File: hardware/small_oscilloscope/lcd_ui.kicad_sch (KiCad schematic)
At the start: 9 parts, among them SW1 RotaryEncoder_Switch_MP, SW2 RotaryEncoder_Switch_MP, SW3 SW_MEC_5E, SW4 SW_MEC_5E, SW5 SW_MEC_5E

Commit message: 250627 circuit
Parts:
- added D4, D5, D6, D7: LED, LED_THT:LED_D3.0mm, symbol Device:LED
- added R29, R30, R31, R32: 1k, Resistor_SMD:R_0603_1608Metric_Pad0.98x0.95mm_HandSolder, symbol Device:R
- added R35, R36, R37, R40, R41, R42: 10k, Resistor_SMD:R_0402_1005Metric_Pad0.72x0.64mm_HandSolder, symbol Device:R
- added SW1: SW_MEC_5E, Button_Switch_SMD:SW_SPST_CK_KMS2xxGP, symbol Switch:SW_MEC_5E
- R33: renamed from R30; footprint (none) -> Resistor_SMD:R_0402_1005Metric_Pad0.72x0.64mm_HandSolder
- R34: renamed from R29; footprint (none) -> Resistor_SMD:R_0402_1005Metric_Pad0.72x0.64mm_HandSolder
- R38: renamed from R31; footprint (none) -> Resistor_SMD:R_0402_1005Metric_Pad0.72x0.64mm_HandSolder
- R39: renamed from R32; footprint (none) -> Resistor_SMD:R_0402_1005Metric_Pad0.72x0.64mm_HandSolder
- renumbered SW1 to SW2, SW5 to SW4, SW4 to SW5, SW2 to SW6
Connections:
- net +3.3V: now also R29.2, R30.2, R31.2, R32.2, R35.1, R36.1, R37.1, R40.1, R41.1, R42.1
- net GND: now also SW2.MP, SW2.S2, SW3.3 (K), SW3.4 (A), SW4.3 (K), SW4.4 (A), SW5.3 (K), SW5.4 (A), SW6.MP, SW6.S2, SW1.3 (K), SW1.4 (A)
- net RE1A: now reaches R39.2, SW6.A
- net RE0A: now reaches R34.2, SW2.A
- net RE0B: now reaches R33.2, SW2.B
- net RE0P: now reaches SW2.S1
- net RE0P: now also R36.2
- net RE1B: now reaches R38.2, SW6.B
- net SW2: now reaches SW4.1
- net SW2: now also SW4.2, R40.2
- net SW0: now reaches SW3.1
- net SW0: now also SW3.2, R37.2
- net RE1P: now reaches SW6.S1
- net RE1P: now also R42.2
- net SW1: now reaches SW5.1
- net SW1: now also SW5.2, R41.2
- new net: D5.1 (K), R30.1
- new net: D4.1 (K), R29.1
- new net: D6.1 (K), R31.1
- new net: D7.1 (K), R32.1
- new net LED0: D4.2 (A)
- new net LED1: D5.2 (A)
- new net LEDRE0: D6.2 (A)
- new net LEDRE1: D7.2 (A)
- new net SW3: R35.2, SW1.1, SW1.2
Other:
- note added: "General-purpose SW 1"
- note added: "SIGNAL DETECT OFF / AUTO / RISE / FALL"
- note added: "SOURCE DC / AC / GND"
- note added: "START / STOP"
- note added: "Time Div / Pos"
- note added: "Voltage Div / Pos"
- moved on the sheet: R33, R34, R38, R39, SW2, SW6

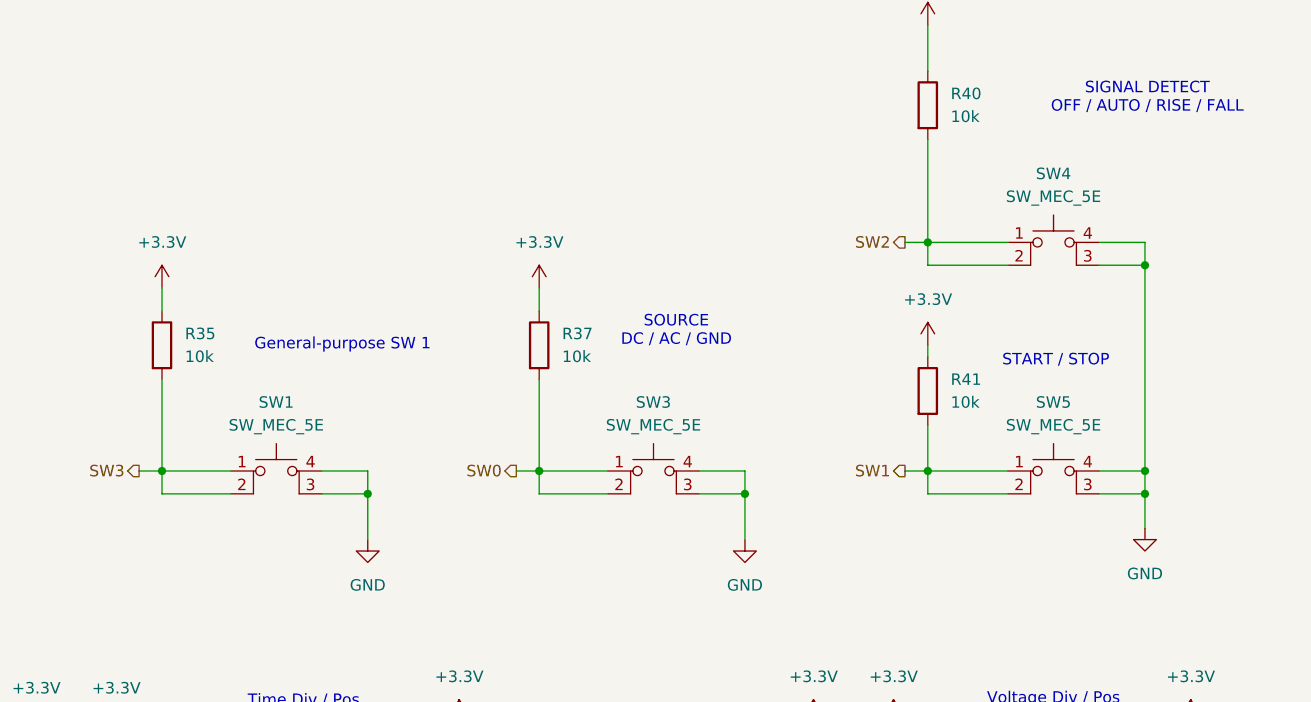
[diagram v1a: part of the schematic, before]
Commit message: feat: 오실로스코프 회로 설계 업데이트
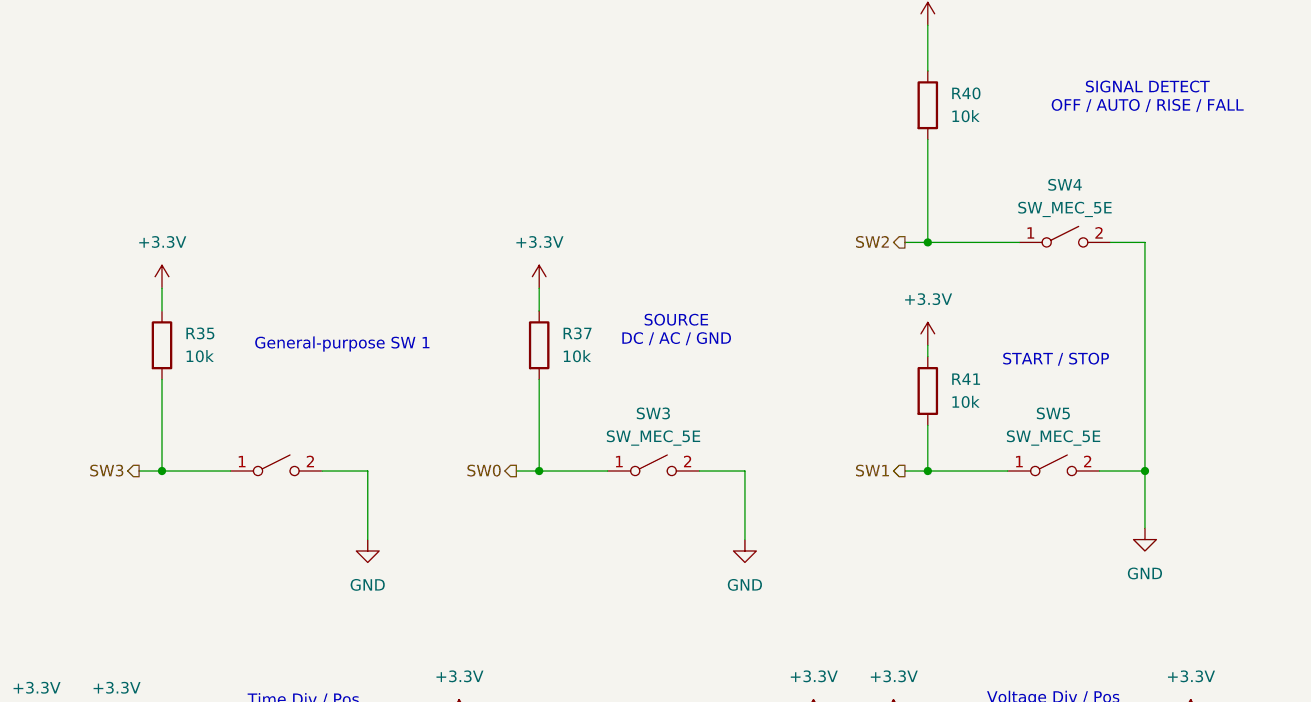
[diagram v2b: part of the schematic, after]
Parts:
- SW1, SW3, SW4, SW5: footprint Button_Switch_SMD:SW_SPST_CK_KMS2xxGP -> Button_Switch_THT:SW_PUSH_6mm_H4.3mm; symbol Switch:SW_MEC_5E -> Switch:SW_SPST
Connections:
- net GND: now also SW1.2 (B), SW3.2 (B), SW4.2 (B), SW5.2 (B); no longer SW1.3 (K), SW1.4 (A), SW3.3 (K), SW3.4 (A), SW4.3 (K), SW4.4 (A), SW5.3 (K), SW5.4 (A)
- net SW0: no longer SW3.2
- net SW1: no longer SW5.2
- net SW2: no longer SW4.2
- net SW3: no longer SW1.2

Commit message: board edit
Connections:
- net LED0: now also D4.1 (K); no longer D4.2 (A)
- net LED1: now also D5.1 (K); no longer D5.2 (A)
- net LEDRE0: now also D6.1 (K); no longer D6.2 (A)
- net LEDRE1: now also D7.1 (K); no longer D7.2 (A)
- net at R30.1: now also D5.2 (A); no longer D5.1 (K)
- net at R29.1: now also D4.2 (A); no longer D4.1 (K)
- net at R31.1: now also D6.2 (A); no longer D6.1 (K)
- net at R32.1: now also D7.2 (A); no longer D7.1 (K)
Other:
- moved on the sheet: D4, D5, D6, D7
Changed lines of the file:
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@@
 	(symbol
 		(lib_id "Device:LED")
-		(at 62.23 66.04 180)
-		(unit 1)
-		(exclude_from_sim no)
-		(in_bom yes)
-		(on_board yes)
-		(dnp no)
-		(fields_autoplaced yes)
+		(at 62.23 66.04 0)
+		(mirror x)
+		(unit 1)
+		(exclude_from_sim no)
+		(in_bom yes)
+		(on_board yes)
+		(dnp no)
 		(property "Reference" "D5"
-			(at 63.8175 58.42 0)
+			(at 60.6425 58.42 0)
 			(effects
 				(font
@@
 		)
 		(property "Value" "LED"
-			(at 63.8175 60.96 0)
+			(at 60.6425 60.96 0)
 			(effects
 				(font
@@
 	(symbol
 		(lib_id "Device:LED")
-		(at 62.23 53.34 180)
-		(unit 1)
-		(exclude_from_sim no)
-		(in_bom yes)
-		(on_board yes)
-		(dnp no)
-		(fields_autoplaced yes)
+		(at 62.23 53.34 0)
+		(mirror x)
+		(unit 1)
+		(exclude_from_sim no)
+		(in_bom yes)
+		(on_board yes)
+		(dnp no)
 		(property "Reference" "D4"
-			(at 63.8175 45.72 0)
+			(at 60.6425 45.72 0)
 			(effects
 				(font
@@
 		)
 		(property "Value" "LED"
-			(at 63.8175 48.26 0)
+			(at 60.6425 48.26 0)
 			(effects
 				(font
@@
 	(symbol
 		(lib_id "Device:LED")
-		(at 62.23 101.6 180)
-		(unit 1)
-		(exclude_from_sim no)
-		(in_bom yes)
-		(on_board yes)
-		(dnp no)
-		(fields_autoplaced yes)
+		(at 62.23 101.6 0)
+		(mirror x)
+		(unit 1)
+		(exclude_from_sim no)
+		(in_bom yes)
+		(on_board yes)
+		(dnp no)
 		(property "Reference" "D7"
-			(at 63.8175 93.98 0)
+			(at 60.6425 93.98 0)
 			(effects
 				(font
@@
 		)
 		(property "Value" "LED"
-			(at 63.8175 96.52 0)
+			(at 60.6425 96.52 0)
 			(effects
 				(font
@@
 	(symbol
 		(lib_id "Device:LED")
-		(at 62.23 90.17 180)
-		(unit 1)
-		(exclude_from_sim no)
-		(in_bom yes)
-		(on_board yes)
-		(dnp no)
-		(fields_autoplaced yes)
+		(at 62.23 90.17 0)
+		(mirror x)
+		(unit 1)
+		(exclude_from_sim no)
+		(in_bom yes)
+		(on_board yes)
+		(dnp no)
 		(property "Reference" "D6"
-			(at 63.8175 82.55 0)
+			(at 60.6425 82.55 0)
 			(effects
 				(font
@@
 		)
 		(property "Value" "LED"
-			(at 63.8175 85.09 0)
-			(effects
-				(font
+			(at 60.6425 85.09 0)
+			(effects
+				(font

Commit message: oscilliscope first success
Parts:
- R66: renamed from R40; now left out of the parts list
- R67: renamed from R29; now left out of the parts list
- R68: renamed from R30; now left out of the parts list
- R69: renamed from R35; now left out of the parts list
- R70: renamed from R37; now left out of the parts list
- R71: renamed from R41; now left out of the parts list
- R72: renamed from R31; now left out of the parts list
- R73: renamed from R32; now left out of the parts list
- R74: renamed from R36; now left out of the parts list
- R75: renamed from R38; now left out of the parts list
- R76: renamed from R39; now left out of the parts list
- R77: renamed from R42; now left out of the parts list
- R78: renamed from R33; now left out of the parts list
- R79: renamed from R34; now left out of the parts list
- renumbered D6 to D10, D7 to D11, D4 to D8, D5 to D9, SW4 to SW1, SW1 to SW2, SW5 to SW4, SW6 to SW5, SW2 to SW6
